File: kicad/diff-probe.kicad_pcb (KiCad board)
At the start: 2 copper layers, 50 x 12 mm, 39 parts, among them IC3 LMH6702, IC4 LMH6702, IC5 LMH6702, J3 HEADER-1X2CARD-EDGE, J4 CON-1X3-TAB-AMP-29173-3-NARROW, X2 SMA--BU-SMA-H

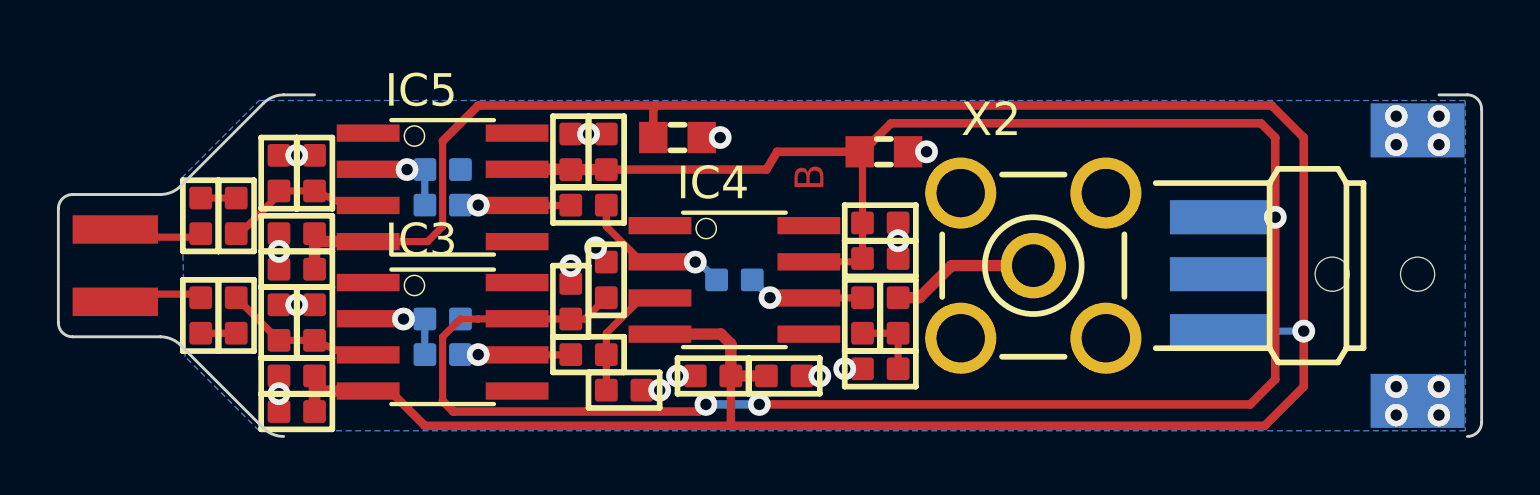
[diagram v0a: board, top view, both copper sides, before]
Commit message: Remove NF resistors and add LCSC part numbers
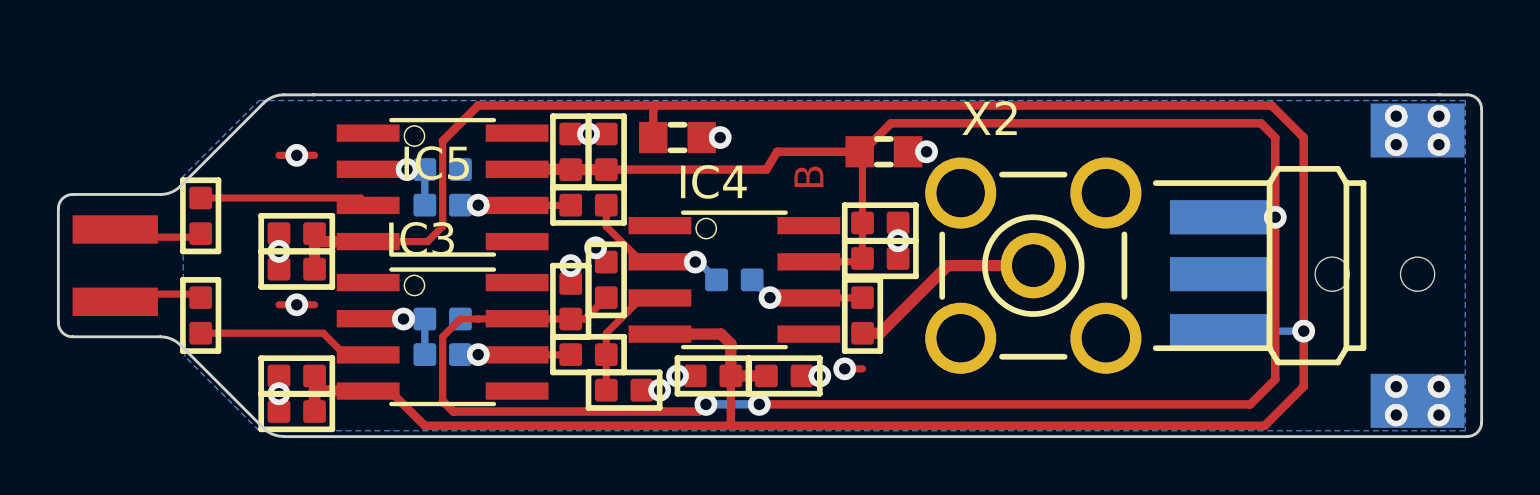
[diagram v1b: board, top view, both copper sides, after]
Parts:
- removed R21, R29, R31: 0Ω/NF, diff-probe:0402-SQUARE
- removed R23, R24, R33, R34, R36: NF, diff-probe:0402-SQUARE
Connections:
- IC3 pad 3: Net-(IC3-Pad3) -> Net-(R20-PadP$2)
- IC5 pad 3: Net-(IC5-Pad3) -> Net-(R28-PadP$2)
- R30 pad P$2: Net-(R30-PadP$2) -> Net-(X2-Pad1)
- X2 pad 1: Net-(R31-PadP$2) -> Net-(X2-Pad1)
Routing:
- net Net-(X2-Pad1): track 0.00 -> 6.98 mm
- net Net-(IC3-Pad3): track 5.72 -> 0.00 mm
- net Net-(R28-PadP$2): track 1.25 -> 6.74 mm
- net Net-(IC5-Pad3): track 5.42 -> 0.00 mm
- net Net-(R31-PadP$2): track 5.22 -> 0.00 mm
- net Net-(R20-PadP$2): track 1.25 -> 6.20 mm
- net Net-(R30-PadP$2): track 2.50 -> 0.00 mm
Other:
- outline, holes or cut-outs redrawn

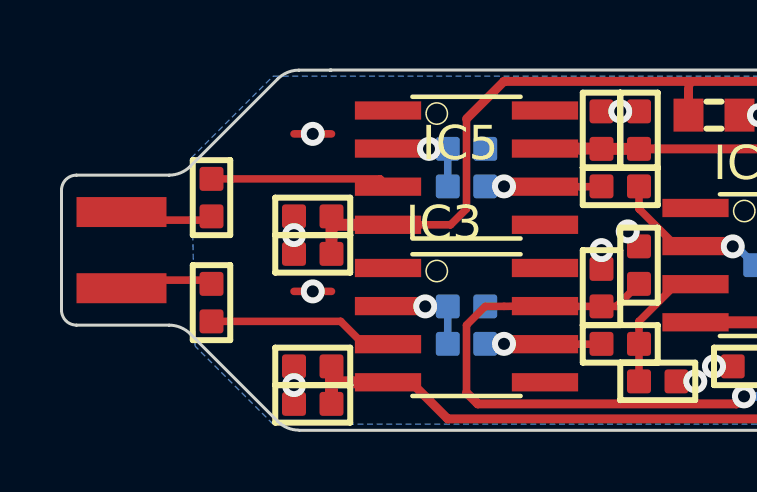
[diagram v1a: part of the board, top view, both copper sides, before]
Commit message: remove NF resistors and rotate input resistors
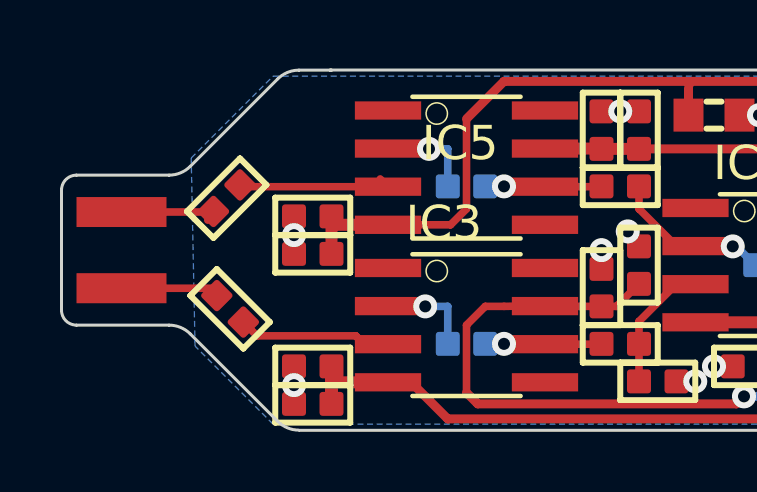
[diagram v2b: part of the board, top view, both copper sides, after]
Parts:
- removed R25, R35: NF, diff-probe:0402-SQUARE
- moved R20 0.65 mm to (129.1, 100.0), turned to -45 degrees
- moved R28 0.51 mm to (129.0, 96.3), turned to 45 degrees
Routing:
- net GND: track 18.6 -> 16.1 mm, vias 22 -> 20
- net Net-(J3-PadP$1): track 3.16 -> 4.44 mm
- net Net-(J3-PadP$2): track 3.16 -> 4.11 mm
- net Net-(R28-PadP$2): track 6.74 -> 6.08 mm

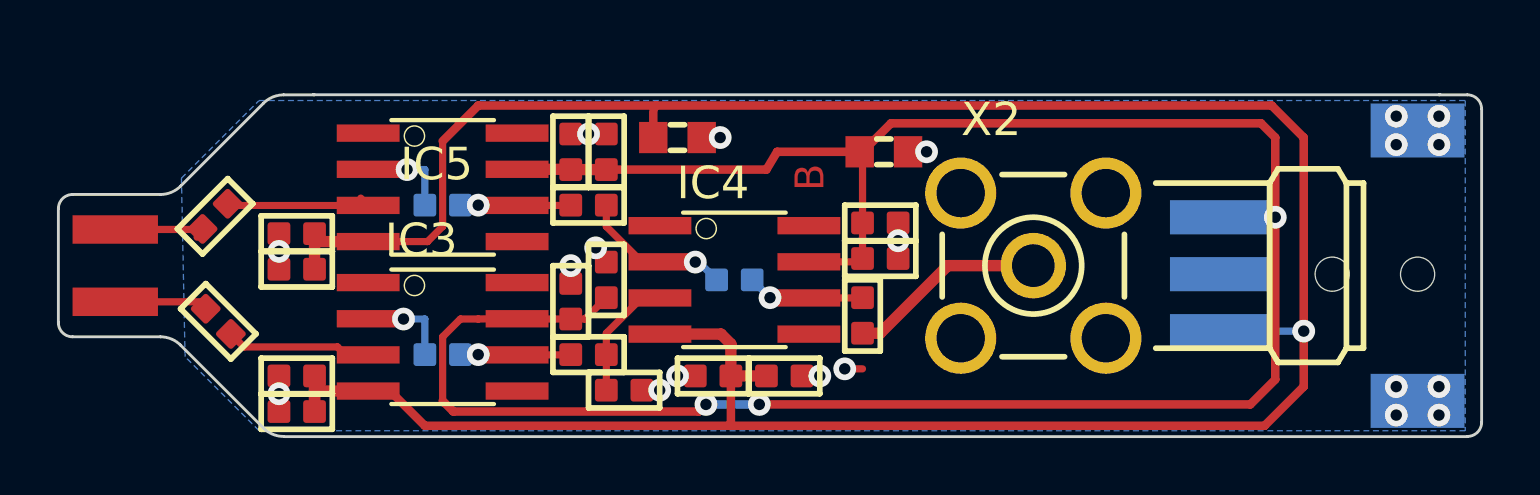
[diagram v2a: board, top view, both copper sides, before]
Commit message: use a better SMA connector
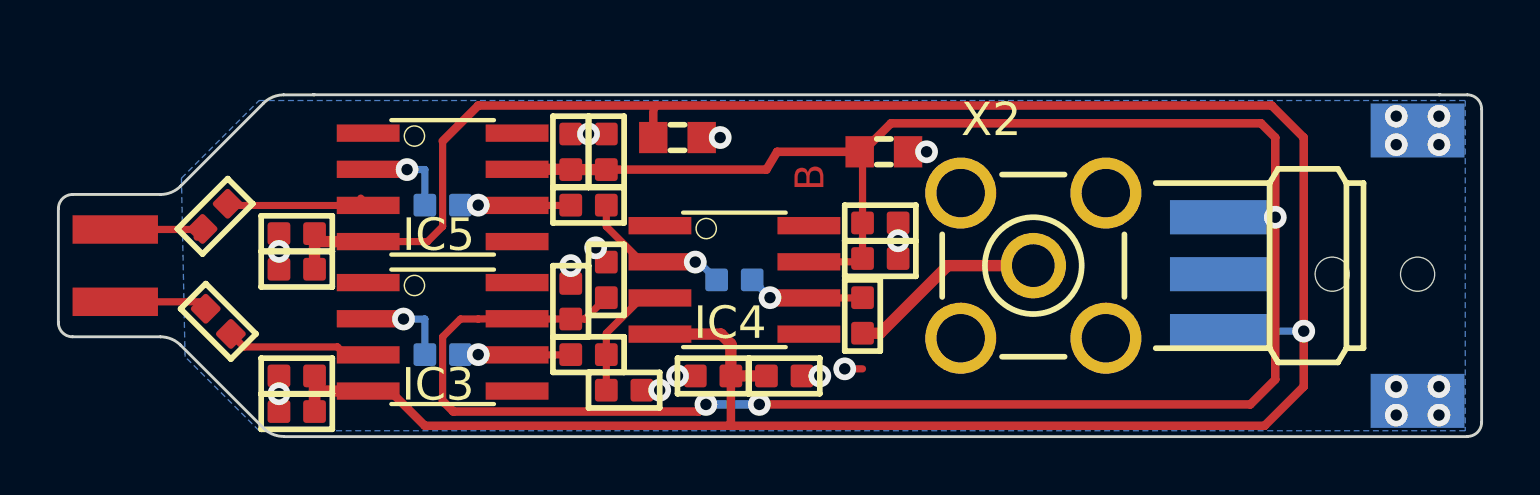
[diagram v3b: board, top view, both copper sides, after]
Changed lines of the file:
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@@
     (property "Sheetfile" "diff-probe.kicad_sch")
     (property "Sheetname" "")
-    (fp_text reference "IC3" (at -2.7305 2.032) (layer "F.SilkS")
+    (fp_text reference "IC3" (at 2.3464 1.4411) (layer "F.SilkS")
       (effects (font (size 1.143 1.143) (thickness 0.127)) (justify left bottom))
     )
@@
     (property "Sheetfile" "diff-probe.kicad_sch")
     (property "Sheetname" "")
-    (fp_text reference "IC5" (at -0.1436 1.4911) (layer "F.SilkS")
+    (fp_text reference "IC5" (at 2.3364 1.4211) (layer "F.SilkS")
       (effects (font (size 1.143 1.143) (thickness 0.127)) (justify left bottom))
     )
@@
     (at 157.7511 98.0036)
     (descr "FEMALE <b>SMA CONNECTOR</b><p>\nRadiall<p>")
-    (property "LCSC" "C1509224")
+    (property "LCSC" "C1509230")
     (property "Sheetfile" "diff-probe.kicad_sch")
     (property "Sheetname" "")
@@
     (property "Sheetfile" "diff-probe.kicad_sch")
     (property "Sheetname" "")
-    (fp_text reference "IC4" (at -2.7305 2.032) (layer "F.SilkS")
+    (fp_text reference "IC4" (at 2.1764 1.4311) (layer "F.SilkS")
       (effects (font (size 1.143 1.143) (thickness 0.127)) (justify left bottom))
     )

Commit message: fix DRC (edge cuts and closeness of trace to letter)
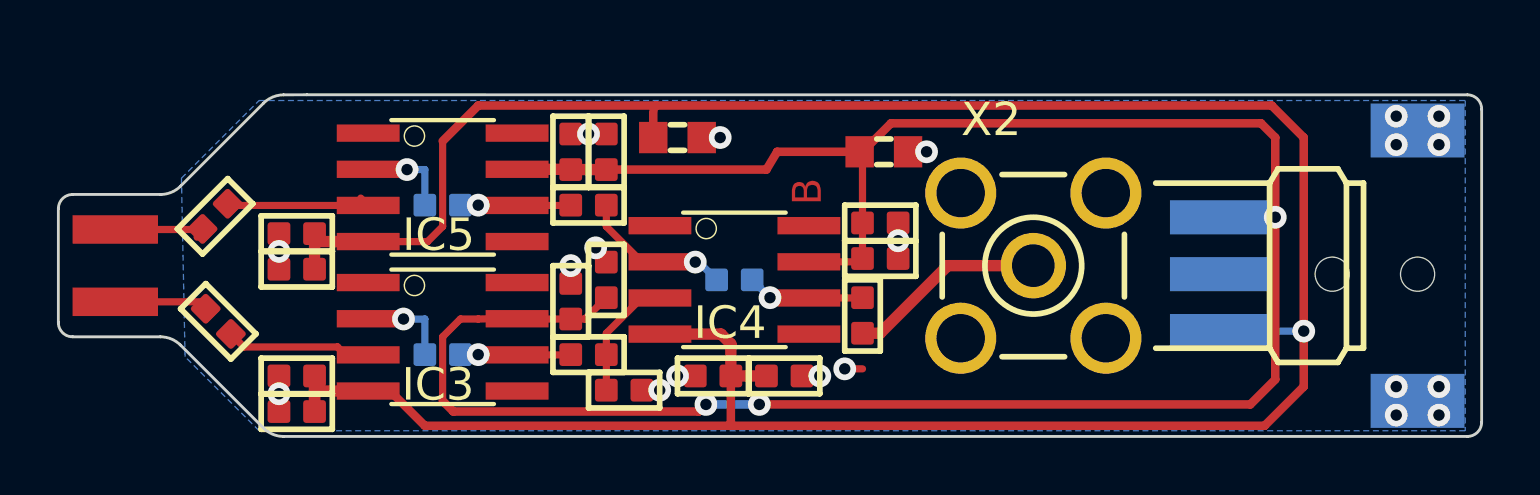
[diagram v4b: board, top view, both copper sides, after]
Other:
- outline, holes or cut-outs redrawn
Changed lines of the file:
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@@
   (gr_line (start 123.5011 100.0036) (end 123.5011 96.0036) (layer "Edge.Cuts") (width 0.1))
   (gr_arc (start 173.5011 103.5036) (mid 173.354653 103.857153) (end 173.0011 104.0036) (layer "Edge.Cuts") (width 0.1))
-  (gr_line (start 131.44 104.01) (end 173.01 104.01) (layer "Edge.Cuts") (width 0.1))
+  (gr_line (start 131.415312 104.0036) (end 173.0011 104.0036) (layer "Edge.Cuts") (width 0.1))
   (gr_arc (start 127.793992 95.210707) (mid 127.46957 95.42748) (end 127.086887 95.5036) (layer "Edge.Cuts") (width 0.1))
   (gr_line (start 130.708206 92.296494) (end 127.793993 95.210707) (layer "Edge.Cuts") (width 0.1))
-  (gr_line (start 132.45 92) (end 172.05 92) (layer "Edge.Cuts") (width 0.1))
+  (gr_line (start 132.23 92) (end 173.0011 92.0036) (layer "Edge.Cuts") (width 0.1))
   (gr_arc (start 124.0011 100.5036) (mid 123.647547 100.357153) (end 123.5011 100.0036) (layer "Edge.Cuts") (width 0.1))
   (gr_line (start 173.5011 103.5036) (end 173.5011 92.5036) (layer "Edge.Cuts") (width 0.1))
-  (gr_line (start 132.5011 92.0036) (end 131.415312 92.0036) (layer "Edge.Cuts") (width 0.1))
+  (gr_line (start 132.23 92) (end 131.415312 92.0036) (layer "Edge.Cuts") (width 0.1))
   (gr_line (start 127.793993 100.796494) (end 130.708206 103.710707) (layer "Edge.Cuts") (width 0.1))
   (gr_arc (start 173.0011 92.0036) (mid 173.354653 92.150047) (end 173.5011 92.5036) (layer "Edge.Cuts") (width 0.1))
-  (gr_line (start 173.0011 92.0036) (end 172.0011 92.0036) (layer "Edge.Cuts") (width 0.1))
   (gr_line (start 124.0011 100.5036) (end 127.086887 100.5036) (layer "Edge.Cuts") (width 0.1))
   (gr_arc (start 123.5011 96.0036) (mid 123.647547 95.650047) (end 124.0011 95.5036) (layer "Edge.Cuts") (width 0.1))
@@
   (gr_line (start 127.086887 95.5036) (end 124.0011 95.5036) (layer "Edge.Cuts") (width 0.1))
   (gr_arc (start 131.415312 104.0036) (mid 131.032629 103.92748) (end 130.708207 103.710707) (layer "Edge.Cuts") (width 0.1))
-  (gr_text "B" (at 150.5011 95.3786 90) (layer "F.Cu")
+  (gr_text "B" (at 150.41 95.88 90) (layer "F.Cu")
     (effects (font (size 1.016 1.016) (thickness 0.254)) (justify left bottom))
   )

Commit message: give nets names to make the PCB more readable
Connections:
- net Net-(IC3-Pad6) renamed /PosIn1
- net Net-(IC4-Pad2) renamed /NEGMID
- net Net-(IC4-Pad3) renamed /POSMID
- net Net-(IC4-Pad6) renamed /OUT
- net Net-(IC5-Pad6) renamed /NegIn1
- net Net-(J3-PadP$1) renamed /PosPad
- net Net-(J3-PadP$2) renamed /NegPad
- net Net-(R20-PadP$2) renamed /POSIN
- net Net-(R28-PadP$2) renamed /NEGIN

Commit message: optimize output
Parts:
- moved R30 0.84 mm to (152.4, 99.2), turned to 0 degrees
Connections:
- net Net-(R30-PadP$2) renamed /OutPad
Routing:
- net /OutPad: track 6.98 -> 5.25 mm
- net GND: track 16.1 -> 15.5 mm, vias 20 -> 19
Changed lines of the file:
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@@
   (net 18 "unconnected-(IC5-Pad8)")
   (net 19 "/NEGIN")
-  (net 20 "Net-(R30-PadP$2)")
+  (net 20 "/OutPad")
   (net 21 "/PosPad")
   (net 22 "/NegPad")
@@
   )
   (footprint "diff-probe:0402-SQUARE" (layer "F.Cu")
-    (at 151.7511 99.7536 -90)
+    (at 152.4 99.22)
     (property "LCSC" "C477760")
     (property "Sheetfile" "diff-probe.kicad_sch")
     (property "Sheetname" "")
-    (fp_text reference "R30" (at 0 0 -90) (layer "F.Fab")
-      (effects (font (size 0.736 0.736) (thickness 0.064)))
-    )
-    (fp_text value "50Ω" (at 0 0 -90) (layer "F.SilkS") hide
-      (effects (font (size 1.27 1.27) (thickness 0.15)))
-    )
-    (fp_line (start -1.25 0.625) (end 1.25 0.625) (layer "F.SilkS") (width 0.2))
-    (fp_line (start -1.25 -0.625) (end -1.25 0.625) (layer "F.SilkS") (width 0.2))
-    (fp_line (start 1.25 0.625) (end 1.25 -0.625) (layer "F.SilkS") (width 0.2))
-    (fp_line (start 1.25 -0.625) (end -1.25 -0.625) (layer "F.SilkS") (width 0.2))
-    (fp_poly (pts
-        (xy -1.25 0.625)
-        (xy 1.25 0.625)
-        (xy 1.25 -0.625)
-        (xy -1.25 -0.625)
-      ) (layer "F.CrtYd") (width 0) (fill solid))
-    (fp_line (start 1.25 0.625) (end 1.25 -0.625) (layer "F.Fab") (width 0.1))
-    (fp_line (start -1.25 -0.625) (end -1.25 0.625) (layer "F.Fab") (width 0.1))
-    (fp_line (start 1.25 -0.625) (end -1.25 -0.625) (layer "F.Fab") (width 0.1))
-    (fp_line (start -1.25 0.625) (end 1.25 0.625) (layer "F.Fab") (width 0.1))
-    (pad "P$1" smd roundrect (at -0.625 0 270) (size 0.8 0.8) (layers "F.Cu" "F.Paste" "F.Mask") (roundrect_rratio 0.125)
+    (fp_text reference "R30" (at 0 0) (layer "F.Fab")
+      (effects (font (size 0.736 0.736) (thickness 0.064)))
+    )
+    (fp_text value "50Ω" (at 0 0) (layer "F.SilkS") hide
+      (effects (font (size 1.27 1.27) (thickness 0.15)))
+    )
+    (fp_line (start -1.25 0.625) (end 1.25 0.625) (layer "F.SilkS") (width 0.2))
+    (fp_line (start -1.25 -0.625) (end -1.25 0.625) (layer "F.SilkS") (width 0.2))
+    (fp_line (start 1.25 0.625) (end 1.25 -0.625) (layer "F.SilkS") (width 0.2))
+    (fp_line (start 1.25 -0.625) (end -1.25 -0.625) (layer "F.SilkS") (width 0.2))
+    (fp_poly (pts
+        (xy -1.25 0.625)
+        (xy 1.25 0.625)
+        (xy 1.25 -0.625)
+        (xy -1.25 -0.625)
+      ) (layer "F.CrtYd") (width 0) (fill solid))
+    (fp_line (start 1.25 0.625) (end 1.25 -0.625) (layer "F.Fab") (width 0.1))
+    (fp_line (start -1.25 -0.625) (end -1.25 0.625) (layer "F.Fab") (width 0.1))
+    (fp_line (start 1.25 -0.625) (end -1.25 -0.625) (layer "F.Fab") (width 0.1))
+    (fp_line (start -1.25 0.625) (end 1.25 0.625) (layer "F.Fab") (width 0.1))
+    (pad "P$1" smd roundrect (at -0.625 0) (size 0.8 0.8) (layers "F.Cu" "F.Paste" "F.Mask") (roundrect_rratio 0.125)
       (net 13 "/OUT") (pinfunction "1") (pintype "passive") (solder_mask_margin 0.0508))
-    (pad "P$2" smd roundrect (at 0.625 0 90) (size 0.8 0.8) (layers "F.Cu" "F.Paste" "F.Mask") (roundrect_rratio 0.125)
-      (net 20 "Net-(R30-PadP$2)") (pinfunction "2") (pintype "passive") (solder_mask_margin 0.0508))
+    (pad "P$2" smd roundrect (at 0.625 0 180) (size 0.8 0.8) (layers "F.Cu" "F.Paste" "F.Mask") (roundrect_rratio 0.125)
+      (net 20 "/OutPad") (pinfunction "2") (pintype "passive") (solder_mask_margin 0.0508))
   )
   (footprint "diff-probe:0402-SQUARE" (layer "F.Cu")
@@
     (fp_circle (center 0 0) (end 3.1999 0) (layer "F.Fab") (width 0.1) (fill none))
     (pad "1" thru_hole circle (at 0 0) (size 2.3 2.3) (drill 1.5) (layers *.Cu *.Mask)
-      (net 20 "Net-(R30-PadP$2)") (pinfunction "1") (pintype "passive") (solder_mask_margin 0.0508))
+      (net 20 "/OutPad") (pinfunction "1") (pintype "passive") (solder_mask_margin 0.0508))
     (pad "2" thru_hole circle (at -2.5499 -2.5499) (size 2.5 2.5) (drill 1.7) (layers *.Cu *.Mask)
       (net 4 "GND") (pinfunction "2") (pintype "passive") (solder_mask_margin 0.0508))
@@
   (segment (start 146.7511 93.5036) (end 146.1011 93.5036) (width 0.3) (layer "F.Cu") (net 4))
   (segment (start 131.2511 98.1286) (end 131.2511 97.5036) (width 0.254) (layer "F.Cu") (net 4))
-  (segment (start 151.1261 101.6286) (end 151.7511 101.6286) (width 0.254) (layer "F.Cu") (net 4))
   (segment (start 142.3761 97.5036) (end 142.3761 97.3786) (width 0.254) (layer "F.Cu") (net 4))
   (segment (start 144.0011 102.3786) (end 144.6261 102.3786) (width 0.254) (layer "F.Cu") (net 4))
@@
   (via (at 153.0011 97.1286) (size 0.8) (drill 0.4) (layers "F.Cu" "B.Cu") (net 4))
   (via (at 144.6261 102.3786) (size 0.8) (drill 0.4) (layers "F.Cu" "B.Cu") (net 4))
-  (via (at 151.1261 101.6286) (size 0.8) (drill 0.4) (layers "F.Cu" "B.Cu") (net 4))
   (via (at 142.3761 97.3786) (size 0.8) (drill 0.4) (layers "F.Cu" "B.Cu") (net 4))
   (via (at 146.7511 93.5036) (size 0.8) (drill 0.4) (layers "F.Cu" "B.Cu") (net 4))
@@
   (segment (start 134.3849 95.8886) (end 133.6361 95.8886) (width 0.254) (layer "F.Cu") (net 19))
   (segment (start 129.5086 95.8886) (end 134.3849 95.8886) (width 0.25) (layer "F.Cu") (net 19))
-  (segment (start 152.3714 100.3786) (end 151.7511 100.3786) (width 0.4) (layer "F.Cu") (net 20))
+  (segment (start 153.045 99.24) (end 153.025 99.22) (width 0.4) (layer "F.Cu") (net 20))
+  (segment (start 154.7464 98.0136) (end 153.52 99.24) (width 0.4) (layer "F.Cu") (net 20))
+  (segment (start 154.7464 98.0036) (end 154.7464 98.0136) (width 0.4) (layer "F.Cu") (net 20))
+  (segment (start 153.52 99.24) (end 153.045 99.24) (width 0.4) (layer "F.Cu") (net 20))
   (segment (start 157.7511 98.0036) (end 154.7464 98.0036) (width 0.4) (layer "F.Cu") (net 20))
-  (segment (start 154.7464 98.0036) (end 152.3714 100.3786) (width 0.4) (layer "F.Cu") (net 20))
   (segment (start 126.6261 99.0036) (end 126.3561 99.2736) (width 0.254) (layer "F.Cu") (net 21))
   (segment (start 126.3561 99.2736) (end 125.5011 99.2736) (width 0.254) (layer "F.Cu") (net 21))
